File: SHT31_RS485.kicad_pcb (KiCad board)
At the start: 2 copper layers, 37 x 7.8 mm, 33 parts, among them IC1 MP1584EN, J1 Connector, U1 STM32F030F4Px, U2 SHT31-DIS, U3 SP3485EN

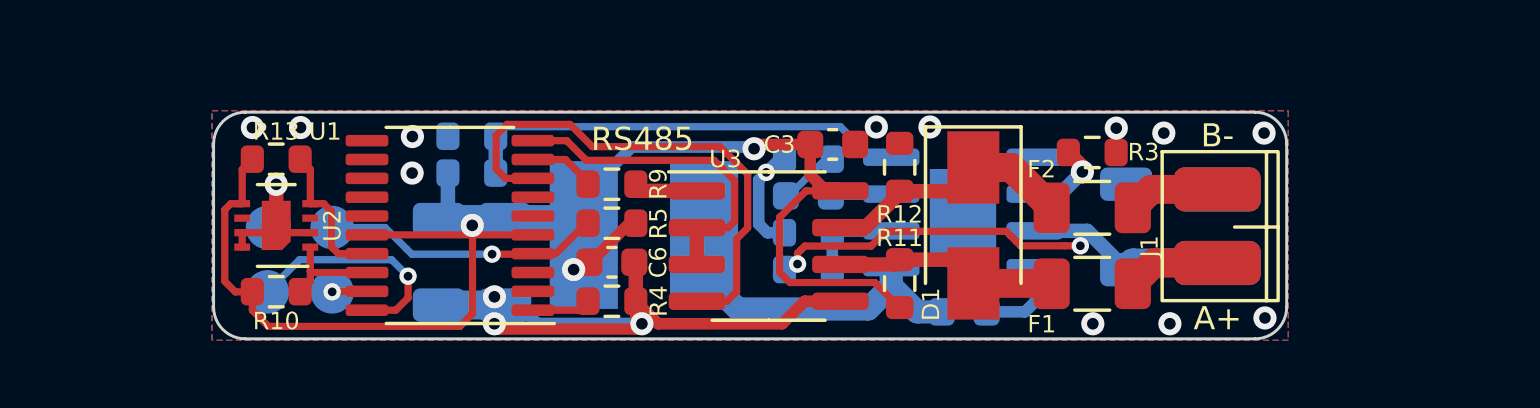
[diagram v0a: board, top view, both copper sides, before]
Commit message: Add MP1584EN Diose.
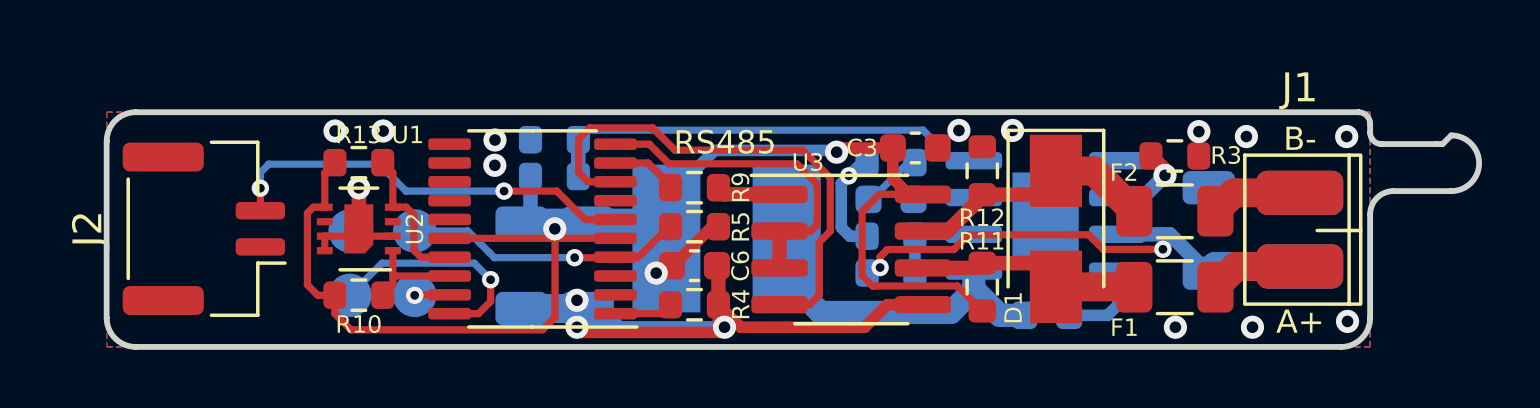
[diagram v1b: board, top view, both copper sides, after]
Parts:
- added J2: ADC, Connector_JST:JST_GH_BM02B-GHS-TBT_1x02-1MP_P1.25mm_Vertical, F.Cu at (129.4, 124.4)
- J1: footprint Conn_Horizontal_2Layer:Conn_02x02_Horizontal_2Layer -> Anh_Footprints:Conn_02x02_Horizontal_2Layer
- moved F1 2.85 mm to (162.9, 126.4)
- moved R11 2.85 mm to (156.2, 126.4)
- moved R12 2.85 mm to (156.2, 122.4)
- moved R4 2.85 mm to (146.3, 127.0)
- moved R5 2.85 mm to (146.3, 124.4)
- moved R9 2.85 mm to (146.3, 123.0)
- moved C6 2.85 mm to (146.3, 125.7)
- moved F2 2.85 mm to (162.9, 123.8)
- moved R3 2.85 mm to (162.9, 121.9)
- moved TP3 2.85 mm to (134.4, 124.5)
- moved C1 2.85 mm to (158.4, 127.4)
- moved C2 2.85 mm to (153.1, 123.4)
- moved C3 2.85 mm to (153.9, 121.6)
- moved C4 2.85 mm to (142.6, 125.7)
- moved C5 2.85 mm to (140.3, 125.7)
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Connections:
- U1 pad 6: unconnected-(U1-Pad6) -> ADC
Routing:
- net ADC: track 0.00 -> 14.5 mm, vias 0 -> 2
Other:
- board size 37 x 7.8 mm -> 47.4 x 8.1 mm
